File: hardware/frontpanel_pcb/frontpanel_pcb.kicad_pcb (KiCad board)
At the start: 2 copper layers, 165 x 40 mm, 19 parts, among them J1 Conn_02x06_Top_Bottom, Q1 BSS138, U1 291V1, U2 NHD-2.8-25664

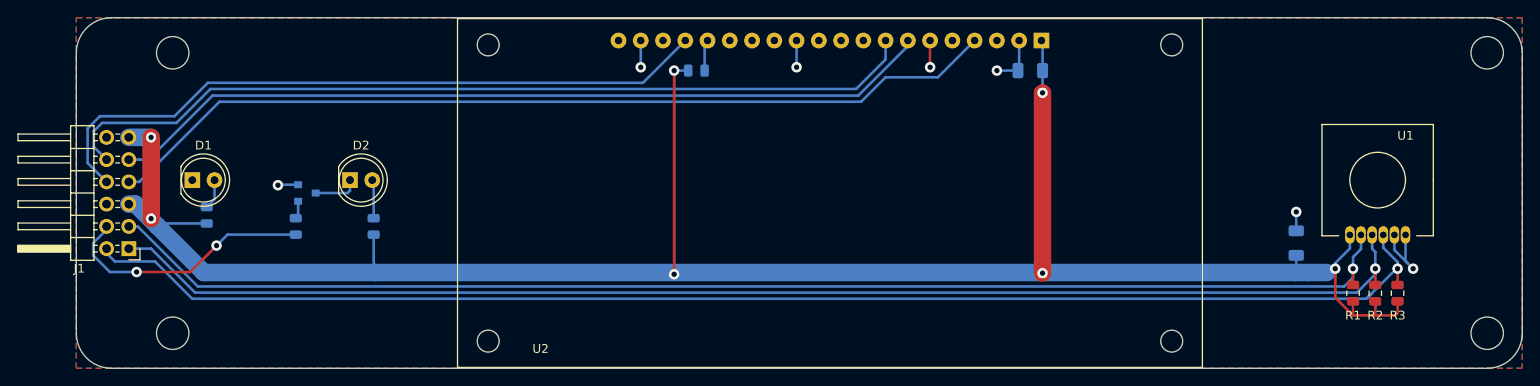
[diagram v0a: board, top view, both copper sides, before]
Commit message: simplified pullups
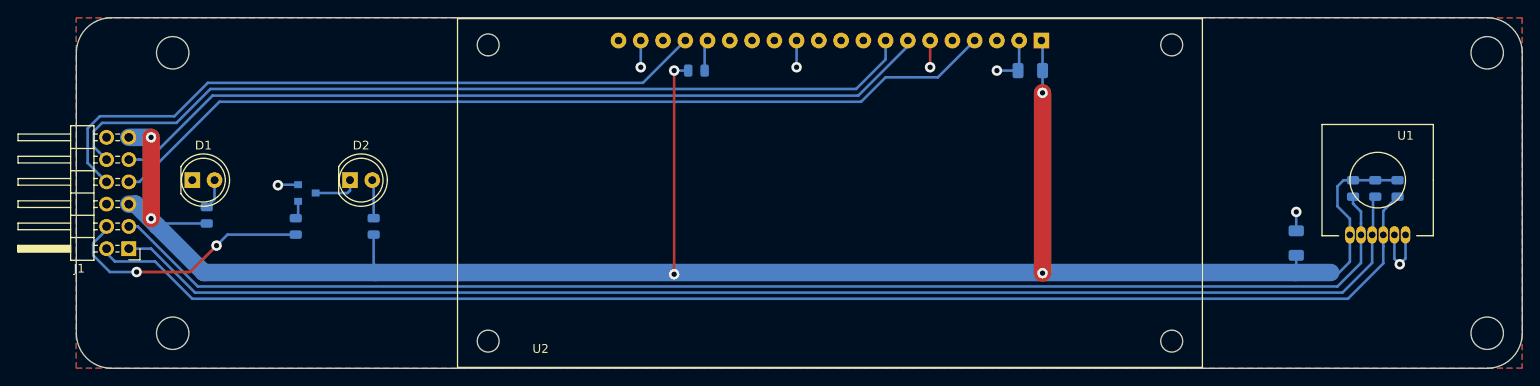
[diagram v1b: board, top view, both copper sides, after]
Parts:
- R1, R2, R3: moved to B.Cu
- moved R1 12.0 mm to (184.7, 79.5), turned to 90 degrees
- moved R2 12.0 mm to (187.2, 79.5), turned to 90 degrees
- moved R3 12.0 mm to (189.8, 79.5), turned to 90 degrees
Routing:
- net /JA3: track 150.1 -> 152.5 mm, vias 1 -> 0
- net +3V3: track 237.1 -> 235.3 mm, vias 7 -> 6
- net /JA1: track 151.7 -> 153.1 mm, vias 1 -> 0
- net GND: track 27.6 -> 26.7 mm
- net /JA2: track 159.1 -> 158.3 mm, vias 1 -> 0

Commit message: Fix display board PMOD pinout
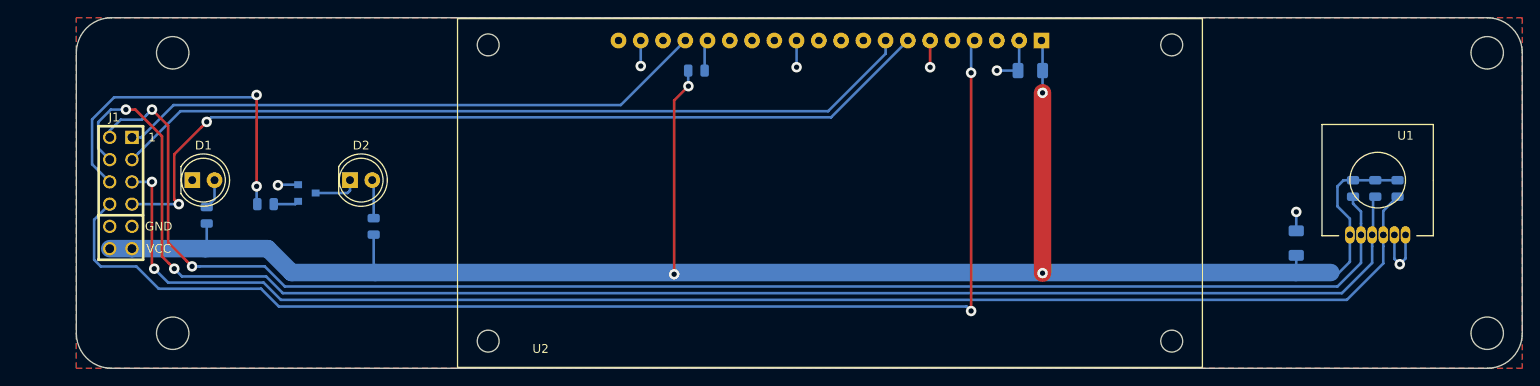
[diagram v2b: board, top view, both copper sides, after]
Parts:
- J1: footprint Connector_PinHeader_2.54mm:PinHeader_2x06_P2.54mm_Horizontal -> pmod-conn_6x2:pmod_pin_array_6x2
- moved J1 6.41 mm to (44.1, 80.0), turned to 0 degrees
- moved R6 4.28 mm to (60.6, 81.3), turned to 0 degrees
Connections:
- J1 pad 11: +3V3 -> GND
- J1 pad 12: GND -> +3V3
- J1 pad 5: +3V3 -> GND
- J1 pad 6: GND -> +3V3
- R1 pad 1: /JA3 -> /JA7
- R2 pad 1: /JA1 -> /JA8
- R3 pad 1: /JA2 -> /JA3
- R6 pad 1: /JA4 -> /JA9
- U1 pad 3: /JA2 -> /JA3
- U1 pad 4: /JA1 -> /JA8
- U1 pad 5: /JA3 -> /JA7
- U2 pad 17: /JA8 -> /JA1
- U2 pad 4: /JA7 -> /JA10
- U2 pad 7: /JA9 -> /JA4
- U2 pad 8: /JA10 -> /JA2
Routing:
- net /JA8: track 79.3 -> 176.6 mm, vias 0 -> 2
- net /JA1: track 153.1 -> 67.7 mm
- net /JA4: track 29.6 -> 101.0 mm
- net /JA7: track 103.2 -> 169.8 mm, vias 0 -> 2
- net /JA2: track 158.3 -> 92.5 mm
- net /JA9: track 94.9 -> 40.4 mm, vias 0 -> 2
- net /JA10: track 99.8 -> 141.0 mm, vias 0 -> 2
- net +3V3: track 235.3 -> 219.8 mm, vias 6 -> 4
- net /JA3: track 152.5 -> 164.0 mm, vias 0 -> 2
- net Net-(Q1-Pad1): track 2.03 -> 2.92 mm

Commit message: frontpanel: update to metric, remove outdated
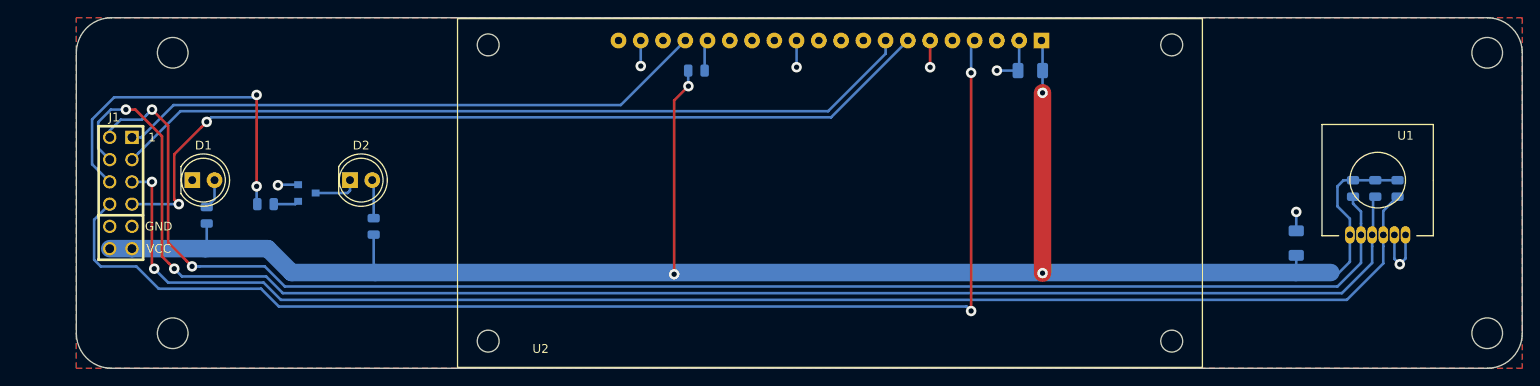
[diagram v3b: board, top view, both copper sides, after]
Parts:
- REF** (x4): value MountingHole_3.7mm -> MountingHole_3.5mm; footprint MountingHole:MountingHole_3.7mm -> MountingHole:MountingHole_3.5mm

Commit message: Move a via out of the way
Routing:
- net /JA3: track 164.0 -> 170.8 mm
- net /JA8: track 176.6 -> 178.3 mm
- net /JA7: track 169.8 -> 171.0 mm

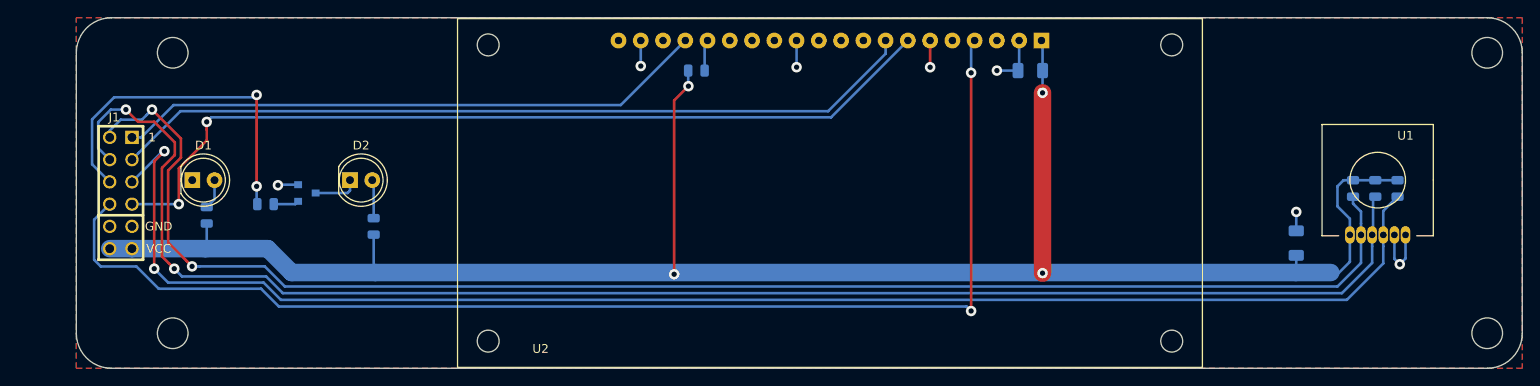
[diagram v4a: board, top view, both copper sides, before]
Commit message: frontpanel_pcb: change mounting holes to 2.5 mm
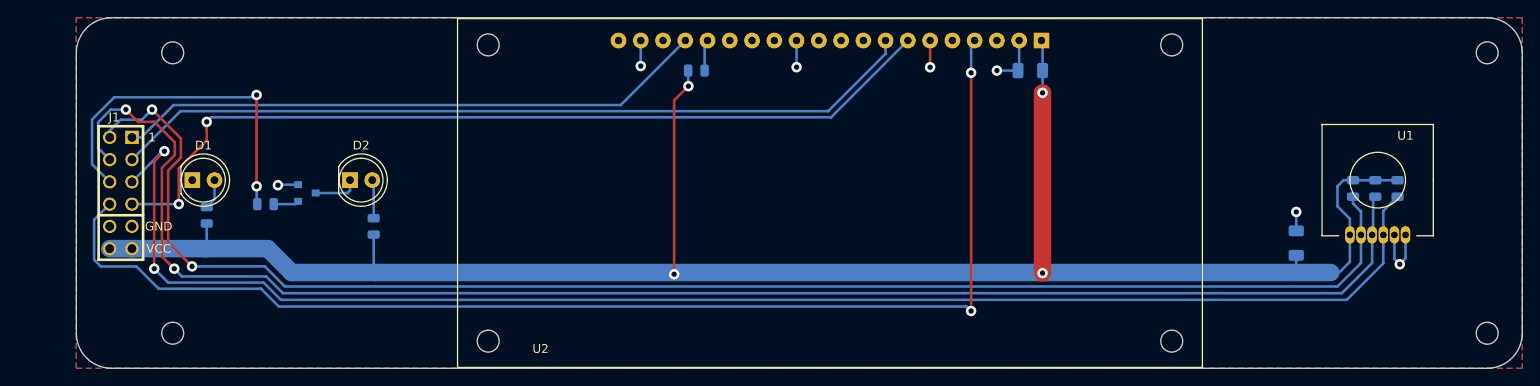
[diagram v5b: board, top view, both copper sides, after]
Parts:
- removed the REF** at (50.0, 64.0)
- removed the REF** at (200.0, 64.0)
- removed the REF** at (50.0, 96.0)
- removed the REF** at (200.0, 96.0)
- added REF**: MountingHole_2.5mm, MountingHole:MountingHole_2.5mm, F.Cu at (50.0, 96.0)
- added REF**: MountingHole_2.5mm, MountingHole:MountingHole_2.5mm, F.Cu at (50.0, 64.0)
- added REF**: MountingHole_2.5mm, MountingHole:MountingHole_2.5mm, F.Cu at (200.0, 64.0)
- added REF**: MountingHole_2.5mm, MountingHole:MountingHole_2.5mm, F.Cu at (200.0, 96.0)
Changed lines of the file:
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@@
-(kicad_pcb (version 20190905) (host pcbnew "(5.99.0-266-g39241dc0f)")
+(kicad_pcb (version 20190907) (host pcbnew "(5.99.0-276-g47d7fea9b)")
   (general
     (thickness 1.6)
@@
     (solder_mask_min_width 0.25)
     (aux_axis_origin 0 0)
-    (grid_origin 41.54 87.62)
+    (grid_origin 50 96)
     (visible_elements FFFFFF7F)
     (pcbplotparams
@@
     (add_net "Net-(U2-Pad9)")
   )
-  (module "MountingHole:MountingHole_3.5mm" locked (layer "F.Cu")
+  (module "MountingHole:MountingHole_2.5mm" locked (layer "F.Cu")
+    (at 50 96)
+    (descr "Mounting Hole 2.5mm, no annular")
+    (tags "mounting hole 2.5mm no annular")
+    (attr virtual)
+    (fp_text reference "REF**" (at 0 -3.5) (layer "F.SilkS") hide
+      (effects (font (size 1 1) (thickness 0.15)))
+    )
+    (fp_text value "MountingHole_2.5mm" (at 0 3.5) (layer "F.Fab") hide
+      (effects (font (size 1 1) (thickness 0.15)))
+    )
+    (fp_circle (center 0 0) (end 2.75 0) (layer "F.CrtYd") (width 0.05))
+    (fp_circle (center 0 0) (end 2.5 0) (layer "Cmts.User") (width 0.15))
+    (fp_text user "%R" (at 0.3 0) (layer "F.Fab")
+      (effects (font (size 1 1) (thickness 0.15)))
+    )
+    (pad "1" np_thru_hole circle (at 0 0) (size 2.5 2.5) (drill 2.5) (layers *.Cu *.Mask))
+  )
+  (module "MountingHole:MountingHole_2.5mm" locked (layer "F.Cu")
     (at 50 64)
-    (descr "Mounting Hole 3.5mm, no annular")
-    (tags "mounting hole 3.5mm no annular")
-    (attr virtual)
-    (fp_text reference "REF**" (at 0 -4.7) (layer "F.SilkS") hide
-      (effects (font (size 1 1) (thickness 0.15)))
-    )
-    (fp_text value "MountingHole_3.5mm" (at 0 4.7) (layer "F.Fab") hide
-      (effects (font (size 1 1) (thickness 0.15)))
-    )
-    (fp_circle (center 0 0) (end 3.75 0) (layer "F.CrtYd") (width 0.05))
-    (fp_circle (center 0 0) (end 3.5 0) (layer "Cmts.User") (width 0.15))
-    (fp_text user "%R" (at 0.3 0) (layer "F.Fab") hide
-      (effects (font (size 1 1) (thickness 0.15)))
-    )
-    (pad "1" np_thru_hole circle (at 0 0) (size 3.5 3.5) (drill 3.5) (layers *.Cu *.Mask))
-  )
-  (module "MountingHole:MountingHole_3.5mm" locked (layer "F.Cu")
+    (descr "Mounting Hole 2.5mm, no annular")
+    (tags "mounting hole 2.5mm no annular")
+    (attr virtual)
+    (fp_text reference "REF**" (at 0 -3.5) (layer "F.SilkS") hide
+      (effects (font (size 1 1) (thickness 0.15)))
+    )
+    (fp_text value "MountingHole_2.5mm" (at 0 3.5) (layer "F.Fab") hide
+      (effects (font (size 1 1) (thickness 0.15)))
+    )
+    (fp_text user "%R" (at 0.3 0) (layer "F.Fab")
+      (effects (font (size 1 1) (thickness 0.15)))
+    )
+    (fp_circle (center 0 0) (end 2.5 0) (layer "Cmts.User") (width 0.15))
+    (fp_circle (center 0 0) (end 2.75 0) (layer "F.CrtYd") (width 0.05))
+    (pad "1" np_thru_hole circle (at 0 0) (size 2.5 2.5) (drill 2.5) (layers *.Cu *.Mask))
+  )
+  (module "MountingHole:MountingHole_2.5mm" locked (layer "F.Cu")
     (at 200 64)
-    (descr "Mounting Hole 3.5mm, no annular")
-    (tags "mounting hole 3.5mm no annular")
-    (attr virtual)
-    (fp_text reference "REF**" (at 0 -4.7) (layer "F.SilkS") hide
-      (effects (font (size 1 1) (thickness 0.15)))
-    )
-    (fp_text value "MountingHole_3.5mm" (at 0 4.7) (layer "F.Fab") hide
-      (effects (font (size 1 1) (thickness 0.15)))
-    )
-    (fp_circle (center 0 0) (end 3.75 0) (layer "F.CrtYd") (width 0.05))
-    (fp_circle (center 0 0) (end 3.5 0) (layer "Cmts.User") (width 0.15))
-    (fp_text user "%R" (at 0.3 0) (layer "F.Fab") hide
-      (effects (font (size 1 1) (thickness 0.15)))
-    )
-    (pad "1" np_thru_hole circle (at 0 0) (size 3.5 3.5) (drill 3.5) (layers *.Cu *.Mask))
-  )
-  (module "MountingHole:MountingHole_3.5mm" locked (layer "F.Cu")
-    (at 50 96)
-    (descr "Mounting Hole 3.5mm, no annular")
-    (tags "mounting hole 3.5mm no annular")
-    (attr virtual)
-    (fp_text reference "REF**" (at 0 -4.7) (layer "F.SilkS") hide
-      (effects (font (size 1 1) (thickness 0.15)))
-    )
-    (fp_text value "MountingHole_3.5mm" (at 0 4.7) (layer "F.Fab") hide
-      (effects (font (size 1 1) (thickness 0.15)))
-    )
-    (fp_circle (center 0 0) (end 3.75 0) (layer "F.CrtYd") (width 0.05))
-    (fp_circle (center 0 0) (end 3.5 0) (layer "Cmts.User") (width 0.15))
-    (fp_text user "%R" (at 0.3 0) (layer "F.Fab") hide
-      (effects (font (size 1 1) (thickness 0.15)))
-    )
-    (pad "1" np_thru_hole circle (at 0 0) (size 3.5 3.5) (drill 3.5) (layers *.Cu *.Mask))
-  )
-  (module "MountingHole:MountingHole_3.5mm" locked (layer "F.Cu")
+    (descr "Mounting Hole 2.5mm, no annular")
+    (tags "mounting hole 2.5mm no annular")
+    (attr virtual)
+    (fp_text reference "REF**" (at 0 -3.5) (layer "F.SilkS") hide
+      (effects (font (size 1 1) (thickness 0.15)))
+    )
+    (fp_text value "MountingHole_2.5mm" (at 0 3.5) (layer "F.Fab") hide
+      (effects (font (size 1 1) (thickness 0.15)))
+    )
+    (fp_circle (center 0 0) (end 2.75 0) (layer "F.CrtYd") (width 0.05))
+    (fp_circle (center 0 0) (end 2.5 0) (layer "Cmts.User") (width 0.15))
+    (fp_text user "%R" (at 0.3 0) (layer "F.Fab")
+      (effects (font (size 1 1) (thickness 0.15)))
+    )
+    (pad "1" np_thru_hole circle (at 0 0) (size 2.5 2.5) (drill 2.5) (layers *.Cu *.Mask))
+  )
+  (module "MountingHole:MountingHole_2.5mm" locked (layer "F.Cu")
     (at 200 96)
-    (descr "Mounting Hole 3.5mm, no annular")
-    (tags "mounting hole 3.5mm no annular")
-    (attr virtual)
-    (fp_text reference "REF**" (at 0 -4.7) (layer "F.SilkS") hide
-      (effects (font (size 1 1) (thickness 0.15)))
-    )
-    (fp_text value "MountingHole_3.5mm" (at 0 4.7) (layer "F.Fab") hide
-      (effects (font (size 1 1) (thickness 0.15)))
-    )
-    (fp_circle (center 0 0) (end 3.75 0) (layer "F.CrtYd") (width 0.05))
-    (fp_circle (center 0 0) (end 3.5 0) (layer "Cmts.User") (width 0.15))
-    (fp_text user "%R" (at 0.3 0) (layer "F.Fab") hide
-      (effects (font (size 1 1) (thickness 0.15)))
-    )
-    (pad "1" np_thru_hole circle (at 0 0) (size 3.5 3.5) (drill 3.5) (layers *.Cu *.Mask))
+    (descr "Mounting Hole 2.5mm, no annular")
+    (tags "mounting hole 2.5mm no annular")
+    (attr virtual)
+    (fp_text reference "REF**" (at 0 -3.5) (layer "F.SilkS") hide
+      (effects (font (size 1 1) (thickness 0.15)))
+    )
+    (fp_text value "MountingHole_2.5mm" (at 0 3.5) (layer "F.Fab") hide
+      (effects (font (size 1 1) (thickness 0.15)))
+    )
+    (fp_text user "%R" (at 0.3 0) (layer "F.Fab")
+      (effects (font (size 1 1) (thickness 0.15)))
+    )
+    (fp_circle (center 0 0) (end 2.5 0) (layer "Cmts.User") (width 0.15))
+    (fp_circle (center 0 0) (end 2.75 0) (layer "F.CrtYd") (width 0.05))
+    (pad "1" np_thru_hole circle (at 0 0) (size 2.5 2.5) (drill 2.5) (layers *.Cu *.Mask))
   )
   (module "pmod-conn_6x2:pmod_pin_array_6x2" (layer "F.Cu")
